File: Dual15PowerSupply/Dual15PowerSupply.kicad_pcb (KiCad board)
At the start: 2 copper layers, 100 x 100 mm, 37 parts, among them J1 120VAC, J2 +/-15VDC, U1 LT3091, U2 LT3081

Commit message: work
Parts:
- moved C6 1.41 mm to (126.2, 123.6)
- moved R9 1.00 mm to (131.1, 120.0)
- moved C8 1.00 mm to (144.0, 112.0)
- moved R11 1.00 mm to (132.0, 127.0)
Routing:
- net /-15VDC: track 0.00 -> 10.6 mm
- net Net-(U1-SET): track 0.00 -> 8.42 mm
- net Net-(U2-SET): track 5.22 -> 10.1 mm
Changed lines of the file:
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@@
 	(footprint "Resistor_SMD:R_1206_3216Metric_Pad1.30x1.75mm_HandSolder"
 		(layer "F.Cu")
-		(at 131 121 90)
+		(at 131.1 120 90)
 		(descr "Resistor SMD 1206 (3216 Metric), square (rectangular) end terminal, IPC-7351 nominal with elongated pad for handsoldering. (Body size source: IPC-SM-782 page 72, https://www.pcb-3d.com/wordpress/wp-content/uploads/ipc-sm-782a_amendment_1_and_2.pdf)")
 		(tags "resistor handsolder")
@@
 	(footprint "Resistor_SMD:R_1206_3216Metric_Pad1.30x1.75mm_HandSolder"
 		(layer "F.Cu")
-		(at 132 128)
+		(at 132 127)
 		(descr "Resistor SMD 1206 (3216 Metric), square (rectangular) end terminal, IPC-7351 nominal with elongated pad for handsoldering. (Body size source: IPC-SM-782 page 72, https://www.pcb-3d.com/wordpress/wp-content/uploads/ipc-sm-782a_amendment_1_and_2.pdf)")
 		(tags "resistor handsolder")
@@
 	(footprint "Capacitor_THT:CP_Radial_D8.0mm_P3.50mm"
 		(layer "F.Cu")
-		(at 143 112 -90)
+		(at 144 112 -90)
 		(descr "CP, Radial series, Radial, pin pitch=3.50mm, diameter=8mm, height=12mm, Electrolytic Capacitor")
 		(tags "CP Radial series Radial pin pitch 3.50mm diameter 8mm height 12mm Electrolytic Capacitor")
 		(property "Reference" "C8"
-			(at 1.75 -5.25 90)
+			(at -3.5 0 0)
 			(layer "F.SilkS")
 			(effects
@@
 		(tags "TO-220-7 Vertical RM 1.27mm staggered type-1")
 		(property "Reference" "U1"
-			(at 4.27 3.8 0)
+			(at 4 -9.6 0)
 			(layer "F.SilkS")
 			(effects
@@
 		)
 		(fp_text user "${REFERENCE}"
-			(at 4.27 3.8 0)
+			(at 4 -9.6 0)
 			(layer "F.Fab")
 			(effects
@@
 		(tags "CP Radial series Radial pin pitch 3.50mm diameter 8mm height 12mm Electrolytic Capacitor")
 		(property "Reference" "C7"
-			(at 1.75 -5.25 90)
+			(at 7 -0.1 180)
 			(layer "F.SilkS")
 			(effects
@@
 	(footprint "Capacitor_THT:C_Rect_L7.2mm_W2.5mm_P5.00mm"
 		(layer "F.Cu")
-		(at 126 125 90)
+		(at 126.2 123.6 90)
 		(descr "C, Rect series, Radial, pin pitch=5.00mm, length*width=7.2*2.5mm^2, Capacitor, R82, https://content.kemet.com/datasheets/KEM_F3101_R82.pdf")
 		(tags "C Rect series Radial pin pitch 5.00mm length 7.2mm width 2.5mm Capacitor R82")
 		(property "Reference" "C6"
-			(at 2.5 -2.5 90)
+			(at 2.5 -3 90)
 			(layer "F.SilkS")
 			(effects
@@
 		)
 		(property "Value" "100nF"
-			(at 2.5 2.5 90)
+			(at -3 -1 180)
 			(layer "F.Fab")
 			(effects
@@
 		(tags "resistor handsolder")
 		(property "Reference" "R7"
-			(at -4 0 90)
+			(at 0 -2.4 90)
 			(layer "F.SilkS")
 			(effects
@@
 	)
 	(segment
+		(start 143.5 115)
+		(end 144 115.5)
+		(width 1.5)
+		(layer "B.Cu")
+		(net "/-15VDC")
+	)
+	(segment
+		(start 133.62 115)
+		(end 143.5 115)
+		(width 1.5)
+		(layer "B.Cu")
+		(net "/-15VDC")
+	)
+	(segment
 		(start 165 109)
 		(end 176.7 109)
@@
 	)
 	(segment
+		(start 169.6 106.4)
+		(end 169.6 111.25)
+		(width 1)
+		(layer "F.Cu")
+		(net "Net-(U2-SET)")
+	)
+	(segment
 		(start 174.77 111.3)
 		(end 169.55 111.3)
@@
 	)
 	(segment
+		(start 169.6 111.25)
+		(end 169.55 111.3)
+		(width 1)
+		(layer "F.Cu")
+		(net "Net-(U2-SET)")
+	)
+	(segment
+		(start 131.08 118.43)
+		(end 131.1 118.45)
+		(width 1)
+		(layer "F.Cu")
+		(net "Net-(U1-SET)")
+	)
+	(segment
+		(start 131.08 115)
+		(end 131.08 118.43)
+		(width 1)
+		(layer "F.Cu")
+		(net "Net-(U1-SET)")
+	)
+	(segment
+		(start 130.95 118.6)
+		(end 131.1 118.45)
+		(width 1)
+		(layer "F.Cu")
+		(net "Net-(U1-SET)")
+	)
+	(segment
+		(start 126.2 118.6)
+		(end 130.95 118.6)
+		(width 1)
+		(layer "F.Cu")
+		(net "Net-(U1-SET)")
+	)
+	(segment

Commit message: Panjit Diode Bridge 3D model
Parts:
- moved R11 1.00 mm to (132.0, 126.0)
- moved D4 0.50 mm to (139.0, 126.0)
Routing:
- net /-15VDC: track 10.6 -> 27.4 mm, vias 0 -> 2
- net Net-(D4-A): track 0.00 -> 2.91 mm
- net /+15VDC: vias 0 -> 1
- added copper zone on B.Cu, net /-15VDC
- added copper zone on F.Cu, net /-15VDC
- added copper zone on B.Cu, net GND
- added copper zone on F.Cu, net GND
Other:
- board text added: "+15V"
- board text added: "-15V"

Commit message: DRC cleanups
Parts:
- moved D1 1.41 mm to (191.0, 62.0)
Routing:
- net /S1: track 35.2 -> 32.9 mm
- net /S2: track 35.2 -> 34.5 mm

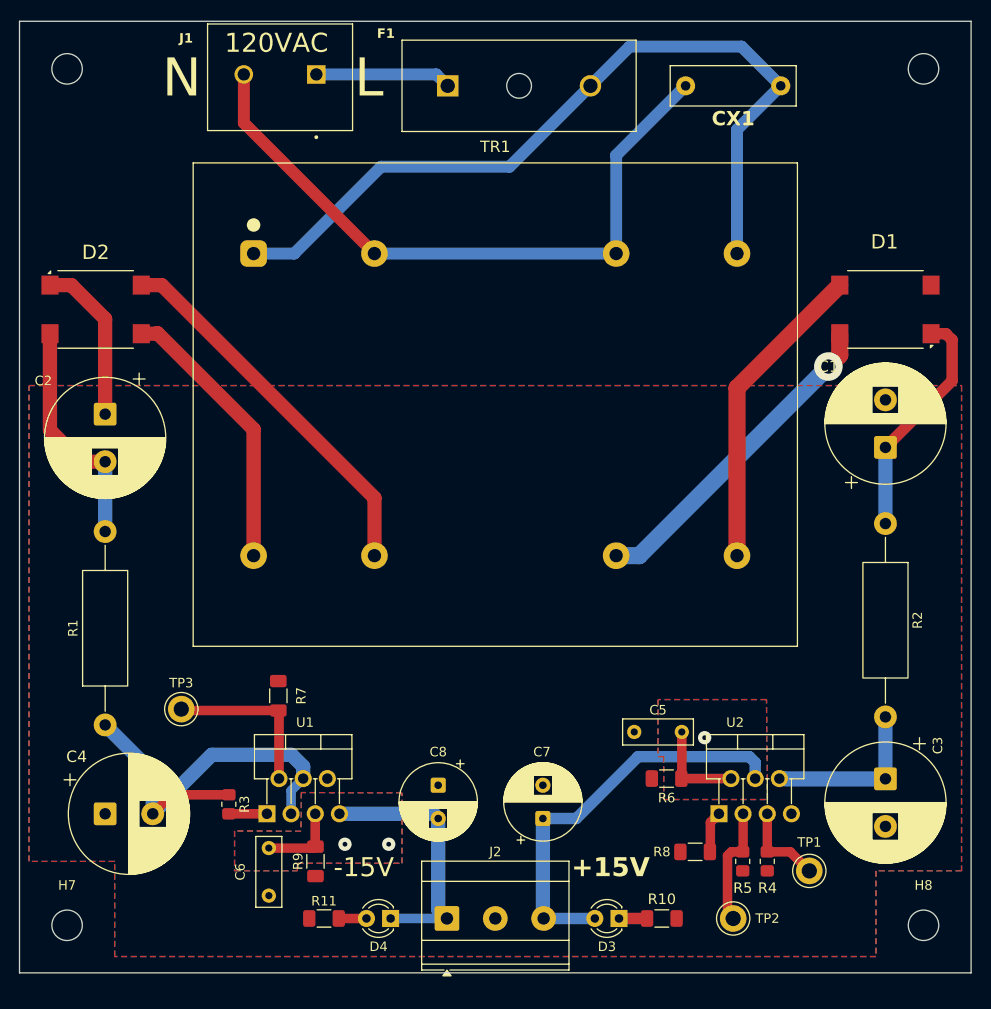
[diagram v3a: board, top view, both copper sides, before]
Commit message: DRC Error cleanups
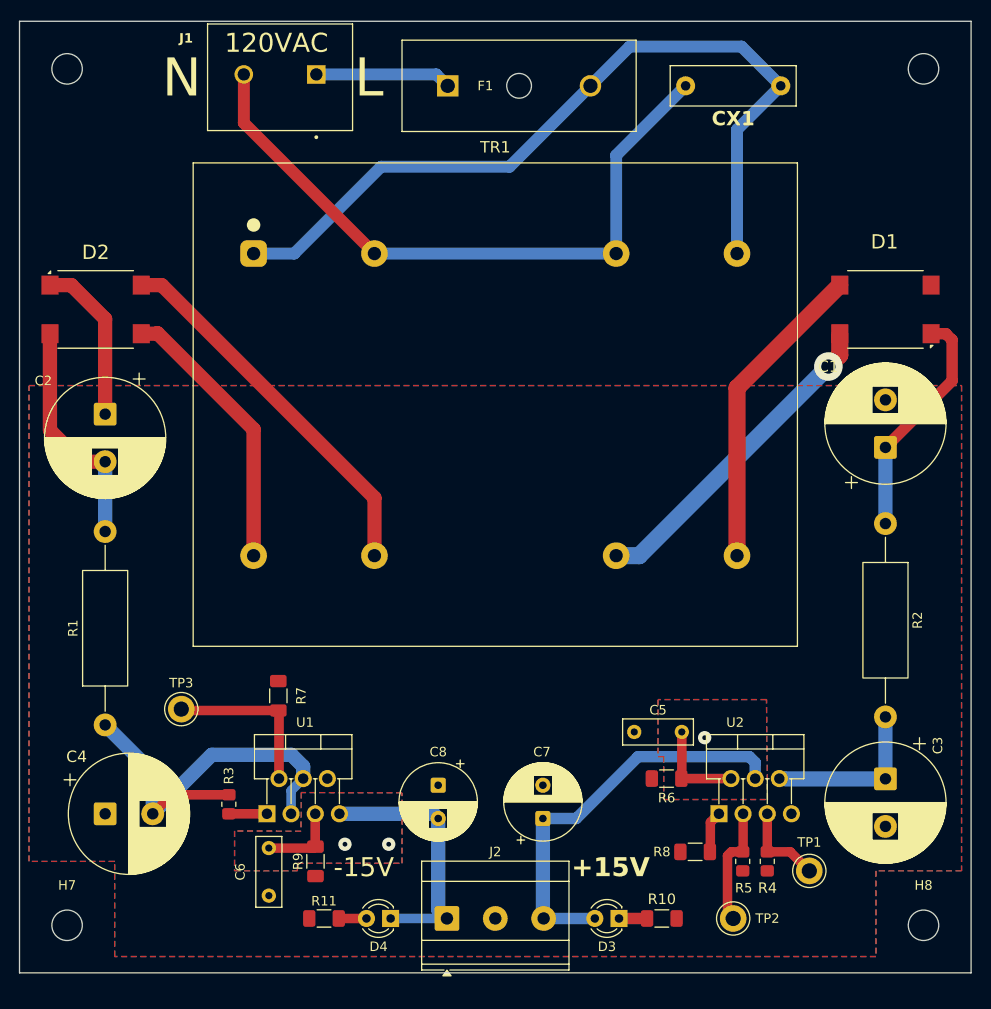
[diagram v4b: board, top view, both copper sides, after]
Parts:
- R3, R5: footprint Resistor_SMD:R_0805_2012Metric_Pad1.20x1.40mm_HandSolder -> Resistor_SMD_JLC:R_0805_2012Metric_Pad1.20x1.40mm_HandSolder

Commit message: DRC fixes
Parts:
- TP1, TP2, TP3: footprint TestPoint:TestPoint_Keystone_5005-5009_Compact -> TestPoint_JLC:TestPoint_Keystone_5005-5009_Compact_JLC
- moved C1 0.50 mm to (191.0, 77.0)
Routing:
- net /RawDC+: track 24.7 -> 25.3 mm

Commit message: DRC cleanup
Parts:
- R10, R11, R6, R7, R8, R9: footprint Resistor_SMD:R_1206_3216Metric_Pad1.30x1.75mm_HandSolder -> Resistor_SMD_JLC:R_1206_3216Metric_Pad1.30x1.75mm_HandSolder
- R4: footprint Resistor_SMD:R_0805_2012Metric_Pad1.20x1.40mm_HandSolder -> Resistor_SMD_JLC:R_0805_2012Metric_Pad1.20x1.40mm_HandSolder
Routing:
- net GND: track 17.3 -> 33.1 mm
- net /+15VDC: track 42.9 -> 55.3 mm, vias 1 -> 2

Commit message: Rev 0.1.4 2026-07-16
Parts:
- J1: footprint TerminalBlock_Phoenix:PHOENIX_1731721 -> TerminalBlock_Phoenix_JLC:PHOENIX_1731721
- moved J2 0.51 mm to (145.0, 125.5)
- moved D3 0.50 mm to (163.0, 125.5)
- moved D4 0.50 mm to (139.0, 125.5)
- moved R10 0.50 mm to (167.5, 125.5)
- moved R11 0.50 mm to (132.0, 125.5)
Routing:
- net /S2: track 34.5 -> 37.9 mm, vias 1 -> 0
- net /S3: track 39.8 -> 43.2 mm
- net /S1: track 32.9 -> 35.8 mm
- net /S4: track 29.3 -> 28.2 mm
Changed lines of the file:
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@@
 	(paper "A4")
 	(title_block
-		(date "2026-07-09")
-		(rev "0.1.3")
+		(date "2026-07-16")
+		(rev "0.1.4")
 	)
 	(layers
@@
 		)
 	)
-	(footprint "TerminalBlock_Phoenix:PHOENIX_1731721"
+	(footprint "TerminalBlock_Phoenix_JLC:PHOENIX_1731721"
 		(layer "F.Cu")
 		(at 135 32 180)
 		(property "Reference" "J1"
-			(at 17.5 -1.5 0)
+			(at 7.5 -5.5 180)
 			(layer "F.SilkS")
 			(effects
 				(font
 					(size 1 1)
-					(thickness 0.18)
-					(bold yes)
+					(thickness 0.15)
 				)
 			)
 		)
 		(property "Value" "120VAC"
-			(at 8 -2 0)
-			(layer "F.SilkS")
+			(at 9.525 -13.035 180)
+			(layer "F.Fab")
 			(effects
 				(font
-					(size 2 2)
-					(thickness 0.2)
+					(size 1 1)
+					(thickness 0.15)
 				)
 			)
 		)
 		(property "Datasheet" ""
-			(at 0 0 0)
+			(at 0 0 180)
 			(layer "F.Fab")
 			(hide yes)
@@
 		)
 		(property "Description" "Generic screw terminal, single row, 01x02, script generated (kicad-library-utils/schlib/autogen/connector/)"
-			(at 0 0 0)
+			(at 0 0 180)
 			(layer "F.Fab")
 			(hide yes)
@@
 	(footprint "Resistor_SMD_JLC:R_1206_3216Metric_Pad1.30x1.75mm_HandSolder"
 		(layer "F.Cu")
-		(at 167.5 126)
+		(at 167.5 125.5)
 		(descr "Resistor SMD 1206 (3216 Metric), square (rectangular) end terminal, IPC-7351 nominal with elongated pad for handsoldering. (Body size source: IPC-SM-782 page 72, https://www.pcb-3d.com/wordpress/wp-content/uploads/ipc-sm-782a_amendment_1_and_2.pdf)")
 		(tags "resistor handsolder")
@@
 	(footprint "TerminalBlock_Phoenix:TerminalBlock_Phoenix_MKDS-3-3-5.08_1x03_P5.08mm_Horizontal"
 		(layer "F.Cu")
-		(at 144.92 126)
+		(at 145 125.5)
 		(descr "Terminal Block Phoenix MKDS-3-3-5.08, 3 pins, pitch 5.08mm, size 15.2x11.2mm, drill diameter 1.3mm, pad diameter 2.6mm, http://www.farnell.com/datasheets/2138224.pdf")
 		(tags "THT Terminal Block Phoenix MKDS-3-3-5.08 pitch 5.08mm size 15.2x11.2mm drill 1.3mm pad 2.6mm")
@@
 	(footprint "Resistor_SMD_JLC:R_1206_3216Metric_Pad1.30x1.75mm_HandSolder"
 		(layer "F.Cu")
-		(at 132 126)
+		(at 132 125.5)
 		(descr "Resistor SMD 1206 (3216 Metric), square (rectangular) end terminal, IPC-7351 nominal with elongated pad for handsoldering. (Body size source: IPC-SM-782 page 72, https://www.pcb-3d.com/wordpress/wp-content/uploads/ipc-sm-782a_amendment_1_and_2.pdf)")
 		(tags "resistor handsolder")
@@
 	(footprint "LED_THT:LED_D3.0mm"
 		(layer "F.Cu")
-		(at 163 126 180)
+		(at 163 125.5 180)
 		(descr "LED, diameter 3.0mm, 2 pins, generated by kicad-footprint-generator")
 		(tags "LED")
@@
 		)
 		(point
-			(at 161.73 126)
+			(at 161.73 125.5)
 			(size 2)
 			(layer "F.Fab")
@@
 		(sheetname "/")
 		(sheetfile "Dual15PowerSupply.kicad_sch")
+		(units
+			(unit
+				(name "A")
+				(pins "1" "2")
+			)
+		)
 		(attr through_hole)
 		(duplicate_pad_numbers_are_jumpers no)
@@
 			)
 		)
+		(model "${KIPRJMOD}/KiCad_WR-FSH (rev26a)/3dmodels/Connector_THT_Wurth.3dshapes/J_Wurth_WR-FSH_696105003002.step"
+			(offset
+				(xyz 0 0 0)
+			)
+			(scale
+				(xyz 1 1 1)
+			)
+			(rotate
+				(xyz 0 0 0)
+			)
+		)
 	)
 	(footprint "Capacitor_THT:CP_Radial_D12.5mm_P5.00mm"
@@
 	(footprint "LED_THT:LED_D3.0mm"
 		(layer "F.Cu")
-		(at 139 126 180)
+		(at 139 125.5 180)
 		(descr "LED, diameter 3.0mm, 2 pins, generated by kicad-footprint-generator")
 		(tags "LED")
@@
 		)
 		(point
-			(at 137.73 126)
+			(at 137.73 125.5)
 			(size 2)
 			(layer "F.Fab")
@@
 	)
 	(segment
-		(start 175.4 87.875)
-		(end 175.4 70.25)
-		(width 1.8)
+		(start 187.95 59.45)
+		(end 188.5 60)
+		(width 1.5)
 		(layer "F.Cu")
 		(net "/S1")
 	)
 	(segment
-		(start 175.4 70.25)
-		(end 186.2 59.45)
-		(width 1.8)
+		(start 186.2 59.45)
+		(end 187.95 59.45)
+		(width 1.5)
 		(layer "F.Cu")
 		(net "/S1")
 	)
 	(segment
-		(start 186.2 64.55)
-		(end 186.2 66.8)
-		(width 1.8)
+		(start 188.5 60)
+		(end 188.5 74.775)
+		(width 1.5)
 		(layer "F.Cu")
-		(net "/S2")
+		(net "/S1")
 	)
 	(segment
-		(start 186.2 66.8)
-		(end 185 68)
+		(start 188.5 74.775)
+		(end 175.4 87.875)
+		(width 1.5)
+		(layer "F.Cu")
+		(net "/S1")
+	)
+	(segment
+		(start 170.625 87.875)
+		(end 186.2 72.3)
 		(width 1.8)
 		(layer "F.Cu")
 		(net "/S2")
 	)
-	(via
-		(at 185 68)
-		(size 3)
-		(drill 1.5)
-		(layers "F.Cu" "B.Cu")
+	(segment
+		(start 162.7 87.875)
+		(end 170.625 87.875)
+		(width 1.8)
+		(layer "F.Cu")
 		(net "/S2")
 	)
 	(segment
-		(start 185 68)
-		(end 165.125 87.875)
-		(width 1.8)
-		(layer "B.Cu")
+		(start 186.2 64.55)
+		(end 186.025 64.55)
+		(width 1.5)
+		(layer "F.Cu")
 		(net "/S2")
 	)
 	(segment
-		(start 165.125 87.875)
-		(end 162.7 87.875)
+		(start 186.2 72.3)
+		(end 186.2 64.55)
 		(width 1.8)
-		(layer "B.Cu")
+		(layer "F.Cu")
 		(net "/S2")
 	)
@@
 	)
 	(segment
-		(start 163 126)
-		(end 165.95 126)
-		(width 1.2)
+		(start 163 125.5)
+		(end 165.95 125.5)
+		(width 1)
 		(layer "F.Cu")
 		(net "Net-(D3-K)")
@@
 	)
 	(segment
-		(start 133.62 115)
-		(end 143.5 115)
-		(width 1.5)
+		(start 139 125.5)
+		(end 145 125.5)
+		(width 1)
 		(layer "B.Cu")
 		(net "/-15VDC")
 	)
 	(segment
-		(start 144 125.08)
-		(end 144.92 126)
+		(start 133.62 115)
+		(end 143.5 115)
 		(width 1.5)
 		(layer "B.Cu")
@@
 	)
 	(segment
-		(start 144 115.5)
-		(end 144 125.08)
+		(start 145 125.5)
+		(end 145 116.5)
 		(width 1.5)
 		(layer "B.Cu")
@@
 	)
 	(segment
-		(start 144.92 126)
-		(end 139 126)
-		(width 1)
+		(start 145 116.5)
+		(end 144 115.5)
+		(width 1.5)
 		(layer "B.Cu")
 		(net "/-15VDC")
@@
 	)
 	(segment
+		(start 155.16 125.5)
+		(end 160.46 125.5)
+		(width 1)
+		(layer "B.Cu")
+		(net "/+15VDC")
+	)
+	(segment
 		(start 165 109)
 		(end 176.7 109)
@@
 	)
 	(segment
-		(start 155.08 126)
-		(end 160.46 126)
-		(width 1.2)
+		(start 155.16 125.5)
+		(end 155.16 115.66)
+		(width 1.5)
 		(layer "B.Cu")
 		(net "/+15VDC")
@@
 	)
 	(segment
-		(start 155 115.5)
-		(end 155 125.92)
-		(width 1.5)
-		(layer "B.Cu")
-		(net "/+15VDC")
-	)
-	(segment
 		(start 158.5 115.5)
 		(end 165 109)
@@
 	)
 	(segment
+		(start 155.16 115.66)
+		(end 155 115.5)
+		(width 1.5)
+		(layer "B.Cu")
+		(net "/+15VDC")
+	)
+	(segment
 		(start 155 115.5)
 		(end 158.5 115.5)
@@
 	)
 	(segment
-		(start 124.6 74.6)
-		(end 114.5 64.5)
-		(width 1.5)
+		(start 112.8 64.55)
+		(end 112.8 76.075)
+		(width 1.8)
 		(layer "F.Cu")
 		(net "/S4")
 	)
 	(segment
-		(start 114.5 64.5)
-		(end 114.45 64.55)
-		(width 1.5)
+		(start 112.8 76.075)
+		(end 124.6 87.875)
+		(width 1.8)
 		(layer "F.Cu")
 		(net "/S4")
 	)
 	(segment
-		(start 124.6 87.875)
-		(end 124.6 74.6)
-		(width 1.5)
+		(start 112.8 60.3)
+		(end 115.5 63)
+		(width 1.6)
 		(layer "F.Cu")
-		(net "/S4")
+		(net "/S3")
 	)
 	(segment
-		(start 114.45 64.55)
-		(end 112.8 64.55)
-		(width 1.5)
+		(start 115.5 63)
+		(end 115.5 74)
+		(width 1.6)
 		(layer "F.Cu")
-		(net "/S4")
+		(net "/S3")
 	)
 	(segment
-		(start 137.3 81.8)
-		(end 114.95 59.45)
-		(width 1.5)
+		(start 115.5 74)
+		(end 129.375 87.875)
+		(width 1.6)
 		(layer "F.Cu")
 		(net "/S3")
 	)
 	(segment
-		(start 137.3 87.875)
-		(end 137.3 81.8)
-		(width 1.5)
+		(start 112.8 59.45)
+		(end 112.8 60.3)
+		(width 1.8)
 		(layer "F.Cu")
 		(net "/S3")
 	)
 	(segment
-		(start 114.95 59.45)
-		(end 112.8 59.45)
-		(width 1.5)
+		(start 129.375 87.875)
+		(end 137.3 87.875)
+		(width 1.6)
 		(layer "F.Cu")
 		(net "/S3")
@@
 	)
 	(segment
-		(start 136.46 126)
-		(end 133.55 126)
+		(start 136.46 125.5)
+		(end 133.55 125.5)
 		(width 1)
 		(layer "F.Cu")
@@
 		)
 		(min_thickness 0.254)
-		(fill yes
+		(fill
 			(thermal_gap 0.508)
 			(thermal_bridge_width 0.508)
@@
 		)
 		(min_thickness 0.3)
-		(fill yes
+		(fill
 			(thermal_gap 0.5)
 			(thermal_bridge_width 0.5)
@@
 		)
 		(min_thickness 0.25)
-		(fill yes
+		(fill
 			(thermal_gap 0.5)
 			(thermal_bridge_width 0.5)

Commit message: Rev number and date in the bottom silk
Ready for Gerbers and pre-production checks.
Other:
- board text added: "Dual15 Supply Andrew Fischer Rev 0.1.4 20260716"
- board text removed: "Dual15 Supply Andrew Fischer 05072026"
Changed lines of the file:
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@@
 		)
 	)
-	(gr_text "Dual15 Supply\nAndrew Fischer\n05072026\n"
+	(gr_text "Dual15 Supply\nAndrew Fischer\nRev 0.1.4 20260716\n"
 		(at 150 81.71562 0)
 		(layer "B.SilkS")
